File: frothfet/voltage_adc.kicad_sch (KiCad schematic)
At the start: 4 parts, among them U23 ADS1015IDGS

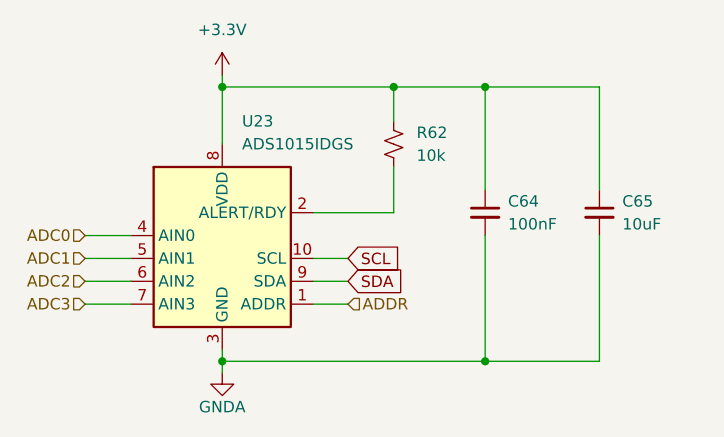
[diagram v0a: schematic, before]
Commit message: fatter power trace and layer 3 is fully ground plane now.
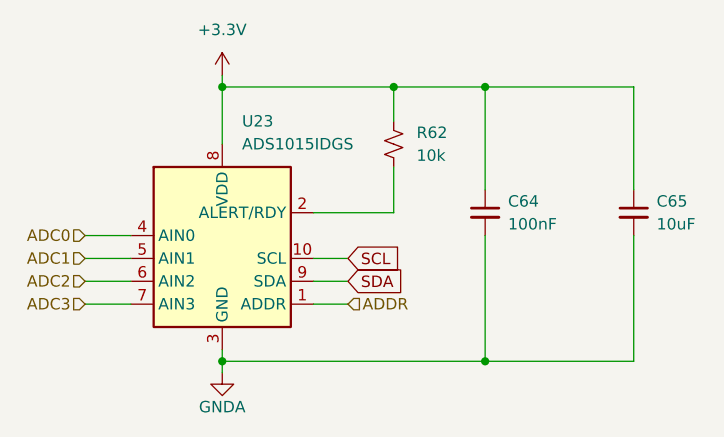
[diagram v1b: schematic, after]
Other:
- moved on the sheet: C65
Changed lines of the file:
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@@
 	(wire
 		(pts
-			(xy 180.34 93.98) (xy 180.34 107.95)
-		)
-		(stroke
-			(width 0)
-			(type default)
-		)
-	)
-	(wire
-		(pts
-			(xy 167.64 77.47) (xy 180.34 77.47)
+			(xy 184.15 93.98) (xy 184.15 107.95)
+		)
+		(stroke
+			(width 0)
+			(type default)
+		)
+	)
+	(wire
+		(pts
+			(xy 167.64 77.47) (xy 184.15 77.47)
 		)
 		(stroke
@@
 	(wire
 		(pts
-			(xy 180.34 77.47) (xy 180.34 88.9)
+			(xy 184.15 77.47) (xy 184.15 88.9)
 		)
 		(stroke
@@
 	(wire
 		(pts
-			(xy 180.34 107.95) (xy 167.64 107.95)
+			(xy 184.15 107.95) (xy 167.64 107.95)
 		)
 		(stroke
@@
 	(symbol
 		(lib_id "Device:C_Small")
-		(at 180.34 91.44 0)
+		(at 184.15 91.44 0)
 		(unit 1)
 		(exclude_from_sim no)
@@
 		(dnp no)
 		(property "Reference" "C65"
-			(at 182.88 90.1763 0)
+			(at 186.69 90.1763 0)
 			(effects
 				(font
@@
 		)
 		(property "Value" "10uF"
-			(at 182.88 92.7163 0)
+			(at 186.69 92.7163 0)
 			(effects
 				(font
@@
 		)
 		(property "Footprint" "Capacitor_SMD:C_0805_2012Metric_Pad1.18x1.45mm_HandSolder"
-			(at 180.34 91.44 0)
+			(at 184.15 91.44 0)
 			(effects
 				(font
@@
 		)
 		(property "Datasheet" "~"
-			(at 180.34 91.44 0)
+			(at 184.15 91.44 0)
 			(effects
 				(font
@@
 		)
 		(property "Description" ""
-			(at 180.34 91.44 0)
+			(at 184.15 91.44 0)
 			(effects
 				(font
@@
 		)
 		(property "Vendor" ""
-			(at 180.34 91.44 0)
+			(at 184.15 91.44 0)
 			(effects
 				(font
@@
 		)
 		(property "LCSC" "C1952580"
-			(at 180.34 91.44 0)
-			(effects
-				(font
+			(at 184.15 91.44 0)
+			(effects
+				(font

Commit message: added selector for 3.3VADC and finalized board.
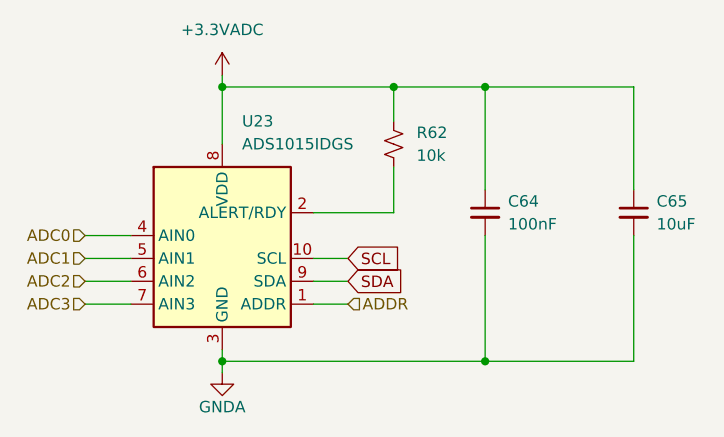
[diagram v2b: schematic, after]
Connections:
- net +3.3V renamed +3.3VADC
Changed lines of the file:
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@@
 	)
 	(symbol
-		(lib_id "power:+3.3V")
+		(lib_id "power:+3.3VADC")
 		(at 138.43 76.2 0)
 		(unit 1)
@@
 		(dnp no)
 		(fields_autoplaced yes)
-		(property "Reference" "#PWR079"
-			(at 138.43 80.01 0)
+		(property "Reference" "#PWR077"
+			(at 142.24 77.47 0)
 			(effects
 				(font
@@
 			)
 		)
-		(property "Value" "+3.3V"
+		(property "Value" "+3.3VADC"
 			(at 138.43 71.12 0)
 			(effects
@@
 			)
 		)
-		(property "Description" "Power symbol creates a global label with name \"+3.3V\""
+		(property "Description" "Power symbol creates a global label with name \"+3.3VADC\""
 			(at 138.43 76.2 0)
 			(effects
@@
 		)
 		(instances
-			(project "8ch-mosfet"
+			(project "frothfet"
 				(path "/c83c6236-96e9-46ad-9d7a-9e2efa4a7966/a6260305-24e3-4714-b441-a7a157c17bd9"
 					(reference "#PWR079")
